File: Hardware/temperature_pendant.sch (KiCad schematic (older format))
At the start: 3 parts

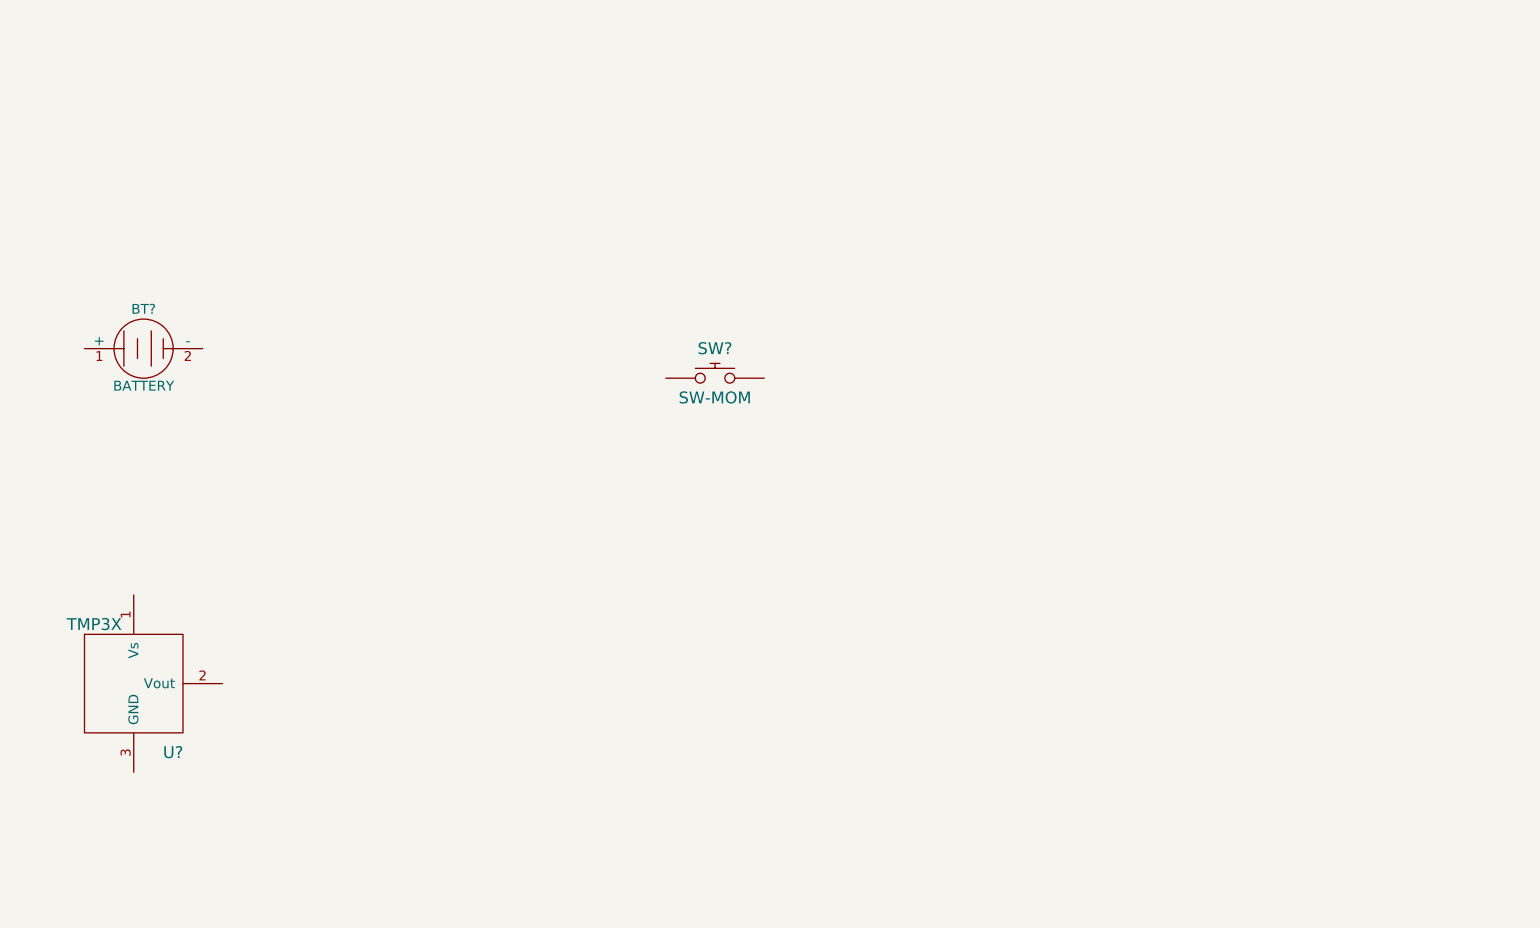
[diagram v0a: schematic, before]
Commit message: Added additional components
Added BlinkM andprogramming header to schematic.
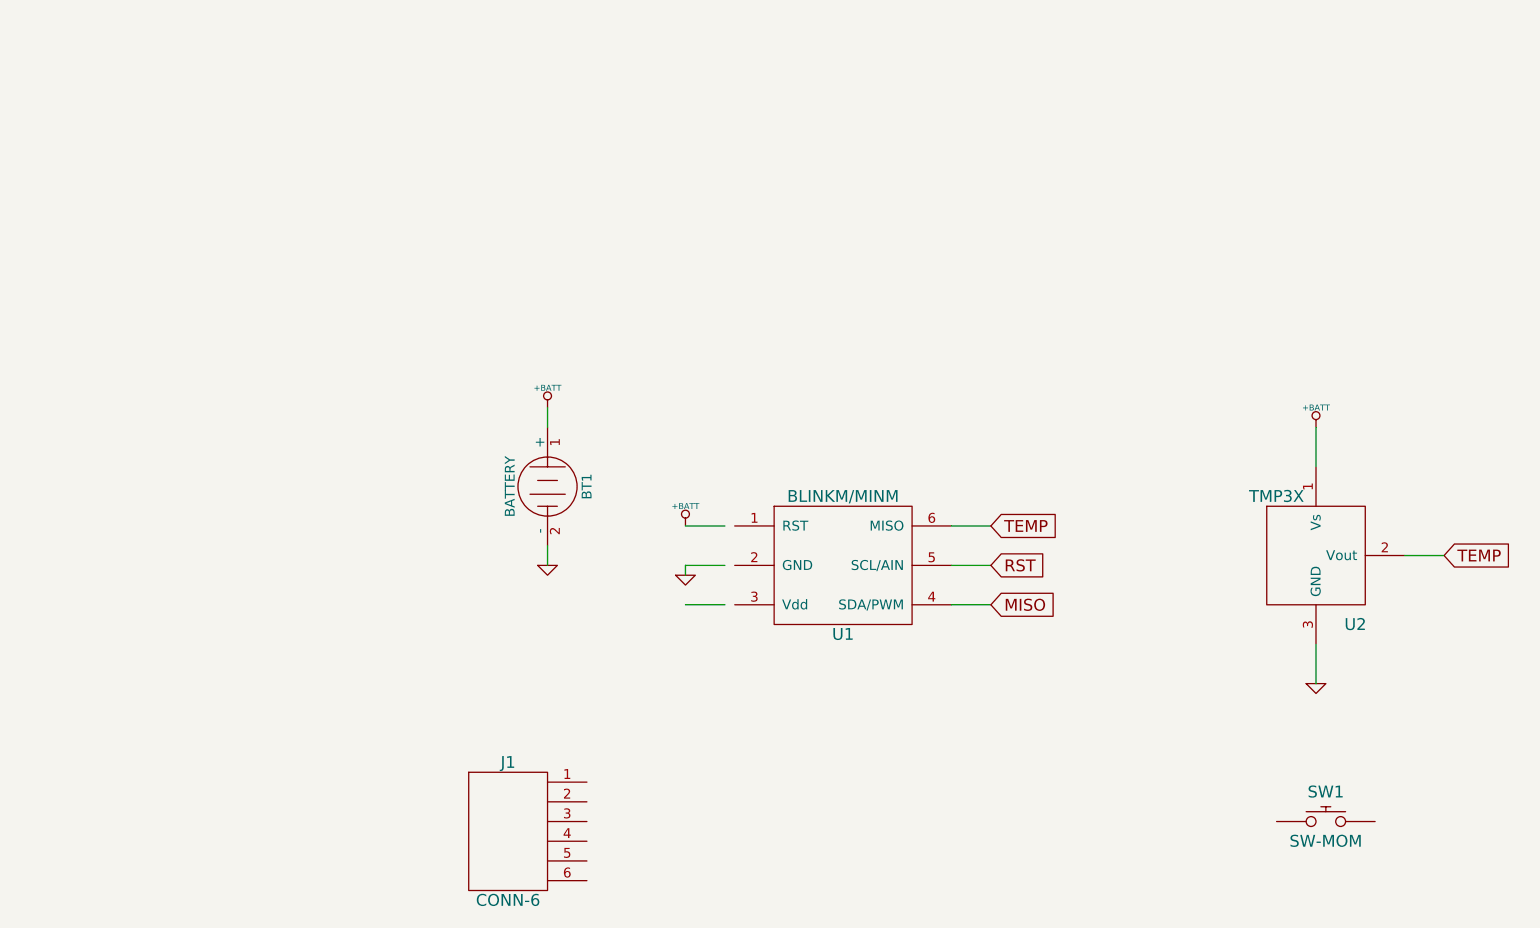
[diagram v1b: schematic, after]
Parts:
- added J1: CONN-6, ~, symbol CONN-6
- added U1: BLINKM/MINM, symbol BLINKM/MINM
- gave numbers to parts that had none: 3
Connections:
- net labels added: +BATT, GND, MISO, RST, TEMP
- wire segments 0 -> 12
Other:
- moved on the sheet: BT1, SW1, U2
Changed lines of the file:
@@
 Sheet 1 1
 Title "Temperature Pendant"
-Date "21 oct 2013"
+Date "22 oct 2013"
 Rev "1"
 Comp "Matthew E. Nelson"
@@
 $EndDescr
 $Comp
-L BATTERY BT?
+L BATTERY BT1
 U 1 1 5264A202
-P 1950 2500
-F 0 "BT?" H 1950 2700 50  0000 C CNN
-F 1 "BATTERY" H 1950 2310 50  0000 C CNN
-F 2 "~" H 1950 2500 60  0000 C CNN
-F 3 "~" H 1950 2500 60  0000 C CNN
-	1    1950 2500
+P 4000 3200
+F 0 "BT1" H 4000 3400 50  0000 C CNN
+F 1 "BATTERY" H 4000 3010 50  0000 C CNN
+F 2 "~" H 4000 3200 60  0000 C CNN
+F 3 "~" H 4000 3200 60  0000 C CNN
+	1    4000 3200
+	0    1    1    0
+$EndComp
+$Comp
+L TMP3X U2
+U 1 1 5264B6FD
+P 7900 3550
+F 0 "U2" H 8100 3200 60  0000 C CNN
+F 1 "TMP3X" H 7700 3850 60  0000 C CNN
+F 2 "" H 7900 3550 60  0000 C CNN
+F 3 "" H 7900 3550 60  0000 C CNN
+	1    7900 3550
 	1    0    0    -1
 $EndComp
 $Comp
-L TMP3X U?
-U 1 1 5264B6FD
-P 1900 4200
-F 0 "U?" H 2100 3850 60  0000 C CNN
-F 1 "TMP3X" H 1700 4500 60  0000 C CNN
-F 2 "" H 1900 4200 60  0000 C CNN
-F 3 "" H 1900 4200 60  0000 C CNN
-	1    1900 4200
+L SW-MOM SW1
+U 1 1 5264B70C
+P 7950 4900
+F 0 "SW1" H 7950 5050 60  0000 C CNN
+F 1 "SW-MOM" H 7950 4800 60  0000 C CNN
+F 2 "~" H 7950 4900 60  0000 C CNN
+F 3 "~" H 7950 4900 60  0000 C CNN
+	1    7950 4900
 	1    0    0    -1
 $EndComp
 $Comp
-L SW-MOM SW?
-U 1 1 5264B70C
-P 4850 2650
-F 0 "SW?" H 4850 2800 60  0000 C CNN
-F 1 "SW-MOM" H 4850 2550 60  0000 C CNN
-F 2 "~" H 4850 2650 60  0000 C CNN
-F 3 "~" H 4850 2650 60  0000 C CNN
-	1    4850 2650
+L BLINKM/MINM U1
+U 1 1 5265EB43
+P 5500 3700
+F 0 "U1" H 5500 3450 60  0000 C CNN
+F 1 "BLINKM/MINM" H 5500 4150 60  0000 C CNN
+F 2 "" H 5500 3700 60  0000 C CNN
+F 3 "" H 5500 3700 60  0000 C CNN
+	1    5500 3700
 	1    0    0    -1
 $EndComp
+Wire Wire Line
+	4000 3500 4000 3600
+$Comp
+L GND #PWR2
+U 1 1 5265EE24
+P 4000 3600
+F 0 "#PWR2" H 4000 3600 30  0001 C CNN
+F 1 "GND" H 4000 3530 30  0001 C CNN
+F 2 "" H 4000 3600 60  0000 C CNN
+F 3 "" H 4000 3600 60  0000 C CNN
+	1    4000 3600
+	1    0    0    -1
+$EndComp
+Wire Wire Line
+	4000 2900 4000 2800
+$Comp
+L +BATT #PWR1
+U 1 1 5265EE65
+P 4000 2800
+F 0 "#PWR1" H 4000 2750 20  0001 C CNN
+F 1 "+BATT" H 4000 2900 30  0000 C CNN
+F 2 "" H 4000 2800 60  0000 C CNN
+F 3 "" H 4000 2800 60  0000 C CNN
+	1    4000 2800
+	1    0    0    -1
+$EndComp
+Wire Wire Line
+	4700 3400 4900 3400
+Wire Wire Line
+	4700 3600 4900 3600
+Wire Wire Line
+	4700 3800 4900 3800
+$Comp
+L +BATT #PWR3
+U 1 1 5265EF91
+P 4700 3400
+F 0 "#PWR3" H 4700 3350 20  0001 C CNN
+F 1 "+BATT" H 4700 3500 30  0000 C CNN
+F 2 "" H 4700 3400 60  0000 C CNN
+F 3 "" H 4700 3400 60  0000 C CNN
+	1    4700 3400
+	1    0    0    -1
+$EndComp
+$Comp
+L GND #PWR4
+U 1 1 5265EFA0
+P 4700 3650
+F 0 "#PWR4" H 4700 3650 30  0001 C CNN
+F 1 "GND" H 4700 3580 30  0001 C CNN
+F 2 "" H 4700 3650 60  0000 C CNN
+F 3 "" H 4700 3650 60  0000 C CNN
+	1    4700 3650
+	1    0    0    -1
+$EndComp
+Wire Wire Line
+	8350 3550 8550 3550
+Text GLabel 8550 3550 2    60   Input ~ 0
+TEMP
+Wire Wire Line
+	7900 4000 7900 4200
+Wire Wire Line
+	7900 2900 7900 3100
+$Comp
+L +BATT #PWR5
+U 1 1 5265F004
+P 7900 2900
+F 0 "#PWR5" H 7900 2850 20  0001 C CNN
+F 1 "+BATT" H 7900 3000 30  0000 C CNN
+F 2 "" H 7900 2900 60  0000 C CNN
+F 3 "" H 7900 2900 60  0000 C CNN
+	1    7900 2900
+	1    0    0    -1
+$EndComp
+$Comp
+L GND #PWR6
+U 1 1 5265F013
+P 7900 4200
+F 0 "#PWR6" H 7900 4200 30  0001 C CNN
+F 1 "GND" H 7900 4130 30  0001 C CNN
+F 2 "" H 7900 4200 60  0000 C CNN
+F 3 "" H 7900 4200 60  0000 C CNN
+	1    7900 4200
+	1    0    0    -1
+$EndComp
+Wire Wire Line
+	4700 3600 4700 3650
+Wire Wire Line
+	6050 3400 6250 3400
+Wire Wire Line
+	6050 3600 6250 3600
+Wire Wire Line
+	6050 3800 6250 3800
+Text GLabel 6250 3400 2    60   Input ~ 0
+TEMP
+Text GLabel 6250 3600 2    60   Input ~ 0
+RST
+Text GLabel 6250 3800 2    60   Input ~ 0
+MISO
+$Comp
+L CONN-6 J1
+U 1 1 5265F63E
+P 3800 4950
+F 0 "J1" H 3800 5300 60  0000 C CNN
+F 1 "CONN-6" H 3800 4600 60  0000 C CNN
+F 2 "~" H 3800 4950 60  0000 C CNN
+F 3 "~" H 3800 4950 60  0000 C CNN
+	1    3800 4950
+	1    0    0    -1
+$EndComp

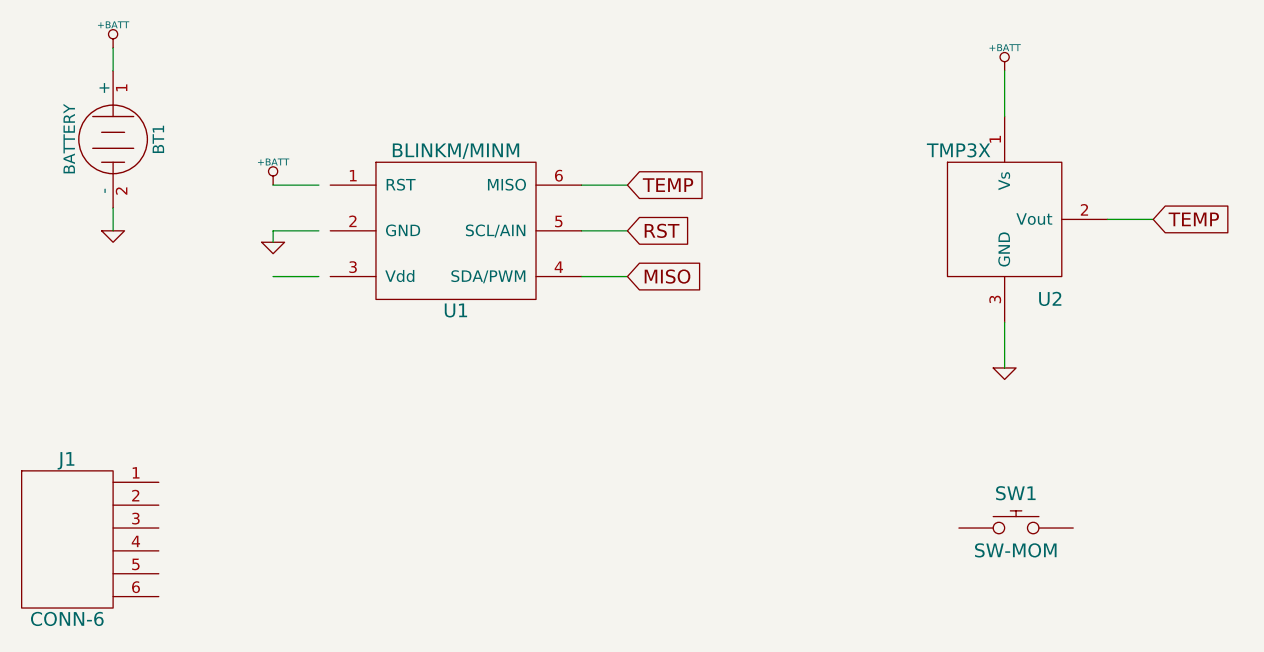
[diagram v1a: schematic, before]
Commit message: Updates
Completed schematic.  Minor revisions, added comments to Arduino code.
Fixed Library reference issue.
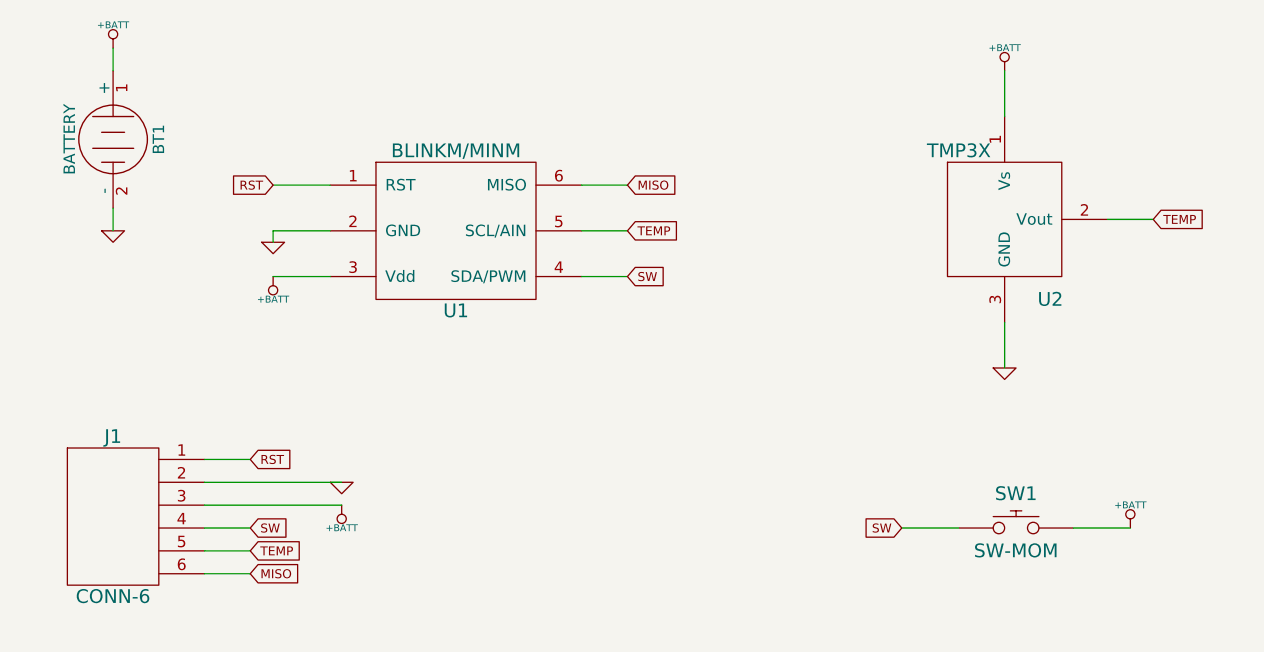
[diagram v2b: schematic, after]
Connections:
- net labels added: SW
- wire segments 12 -> 20
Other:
- moved on the sheet: J1
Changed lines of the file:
@@
 Sheet 1 1
 Title "Temperature Pendant"
-Date "22 oct 2013"
+Date "26 oct 2013"
 Rev "1"
 Comp "Matthew E. Nelson"
@@
 $EndComp
 Wire Wire Line
-	4700 3400 4900 3400
-Wire Wire Line
-	4700 3600 4900 3600
-Wire Wire Line
-	4700 3800 4900 3800
+	4700 3400 4950 3400
+Wire Wire Line
+	4700 3600 4950 3600
+Wire Wire Line
+	4700 3800 4950 3800
 $Comp
 L +BATT #PWR3
 U 1 1 5265EF91
-P 4700 3400
-F 0 "#PWR3" H 4700 3350 20  0001 C CNN
-F 1 "+BATT" H 4700 3500 30  0000 C CNN
-F 2 "" H 4700 3400 60  0000 C CNN
-F 3 "" H 4700 3400 60  0000 C CNN
-	1    4700 3400
-	1    0    0    -1
+P 4700 3800
+F 0 "#PWR3" H 4700 3750 20  0001 C CNN
+F 1 "+BATT" H 4700 3900 30  0000 C CNN
+F 2 "" H 4700 3800 60  0000 C CNN
+F 3 "" H 4700 3800 60  0000 C CNN
+	1    4700 3800
+	1    0    0    1
 $EndComp
 $Comp
@@
 Wire Wire Line
 	8350 3550 8550 3550
-Text GLabel 8550 3550 2    60   Input ~ 0
+Text GLabel 8550 3550 2    39   Input ~ 0
 TEMP
 Wire Wire Line
@@
 Wire Wire Line
 	6050 3800 6250 3800
-Text GLabel 6250 3400 2    60   Input ~ 0
+Text GLabel 6250 3400 2    39   Input ~ 0
+MISO
+Text GLabel 6250 3600 2    39   Input ~ 0
 TEMP
-Text GLabel 6250 3600 2    60   Input ~ 0
-RST
-Text GLabel 6250 3800 2    60   Input ~ 0
-MISO
+Text GLabel 6250 3800 2    39   Input ~ 0
+SW
 $Comp
 L CONN-6 J1
 U 1 1 5265F63E
-P 3800 4950
-F 0 "J1" H 3800 5300 60  0000 C CNN
-F 1 "CONN-6" H 3800 4600 60  0000 C CNN
-F 2 "~" H 3800 4950 60  0000 C CNN
-F 3 "~" H 3800 4950 60  0000 C CNN
-	1    3800 4950
-	1    0    0    -1
-$EndComp
+P 4000 4850
+F 0 "J1" H 4000 5200 60  0000 C CNN
+F 1 "CONN-6" H 4000 4500 60  0000 C CNN
+F 2 "~" H 4000 4850 60  0000 C CNN
+F 3 "~" H 4000 4850 60  0000 C CNN
+	1    4000 4850
+	1    0    0    -1
+$EndComp
+Wire Wire Line
+	7700 4900 7450 4900
+Text GLabel 7450 4900 0    39   Input ~ 0
+SW
+Wire Wire Line
+	8200 4900 8450 4900
+$Comp
+L +BATT #PWR?
+U 1 1 526BECF7
+P 8450 4900
+F 0 "#PWR?" H 8450 4850 20  0001 C CNN
+F 1 "+BATT" H 8450 5000 30  0000 C CNN
+F 2 "" H 8450 4900 60  0000 C CNN
+F 3 "" H 8450 4900 60  0000 C CNN
+	1    8450 4900
+	1    0    0    -1
+$EndComp
+Text GLabel 4700 3400 0    39   Input ~ 0
+RST
+Wire Wire Line
+	4400 4600 4600 4600
+Wire Wire Line
+	4400 4700 5000 4700
+Wire Wire Line
+	4400 4800 5000 4800
+Wire Wire Line
+	4400 4900 4600 4900
+Wire Wire Line
+	4400 5000 4600 5000
+Wire Wire Line
+	4400 5100 4600 5100
+Text GLabel 4600 4600 2    39   Input ~ 0
+RST
+Text GLabel 4600 4900 2    39   Input ~ 0
+SW
+Text GLabel 4600 5000 2    39   Input ~ 0
+TEMP
+Text GLabel 4600 5100 2    39   Input ~ 0
+MISO
+$Comp
+L +BATT #PWR?
+U 1 1 526BEF1C
+P 5000 4800
+F 0 "#PWR?" H 5000 4750 20  0001 C CNN
+F 1 "+BATT" H 5000 4900 30  0000 C CNN
+F 2 "" H 5000 4800 60  0000 C CNN
+F 3 "" H 5000 4800 60  0000 C CNN
+	1    5000 4800
+	1    0    0    1
+$EndComp
+$Comp
+L GND #PWR?
+U 1 1 526BEF30
+P 5000 4700
+F 0 "#PWR?" H 5000 4700 30  0001 C CNN
+F 1 "GND" H 5000 4630 30  0001 C CNN
+F 2 "" H 5000 4700 60  0000 C CNN
+F 3 "" H 5000 4700 60  0000 C CNN
+	1    5000 4700
+	1    0    0    -1
+$EndComp

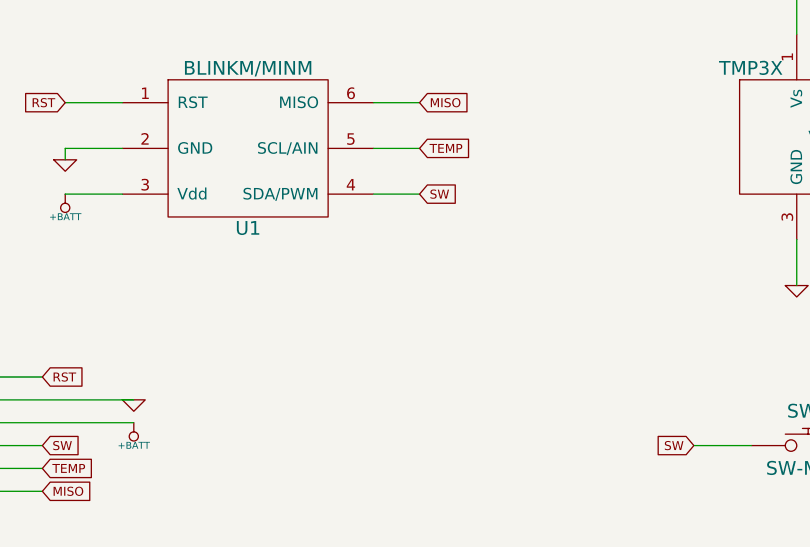
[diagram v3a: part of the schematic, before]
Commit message: Enabled built-in pull ups
Enabled built-in pull down resistor to better stabilize the SW input.
Testing if I still need an external pull-down but for now added one in
the schematic.
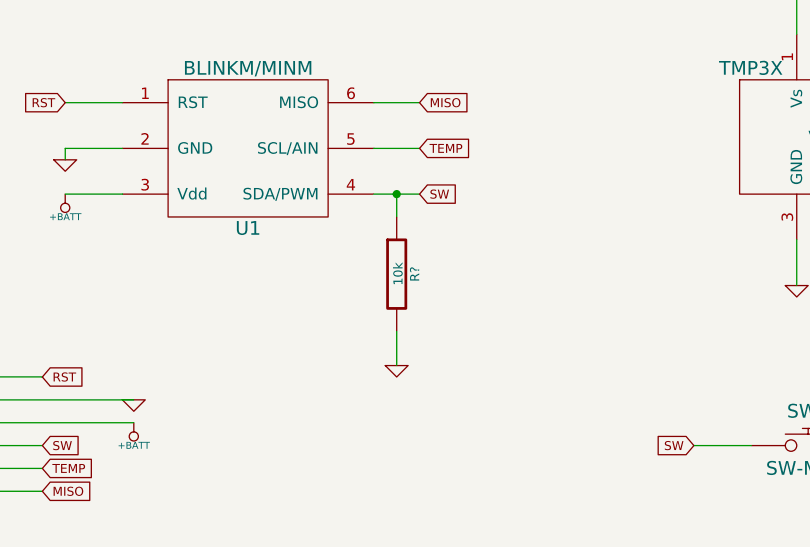
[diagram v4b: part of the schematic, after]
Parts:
- added R?: 10k, ~, symbol R
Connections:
- net GND: now also R?.2
- net SW: now also R?.1
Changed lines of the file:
@@
 Sheet 1 1
 Title "Temperature Pendant"
-Date "26 oct 2013"
+Date "7 dec 2013"
 Rev "1"
 Comp "Matthew E. Nelson"
@@
 	1    0    0    -1
 $EndComp
+$Comp
+L R R?
+U 1 1 52A2BDC6
+P 6150 4150
+F 0 "R?" V 6230 4150 40  0000 C CNN
+F 1 "10k" V 6157 4151 40  0000 C CNN
+F 2 "~" V 6080 4150 30  0000 C CNN
+F 3 "~" H 6150 4150 30  0000 C CNN
+	1    6150 4150
+	1    0    0    -1
+$EndComp
+Wire Wire Line
+	6150 3900 6150 3800
+Connection ~ 6150 3800
+Wire Wire Line
+	6150 4400 6150 4550
+$Comp
+L GND #PWR?
+U 1 1 52A2BE02
+P 6150 4550
+F 0 "#PWR?" H 6150 4550 30  0001 C CNN
+F 1 "GND" H 6150 4480 30  0001 C CNN
+F 2 "" H 6150 4550 60  0000 C CNN
+F 3 "" H 6150 4550 60  0000 C CNN
+	1    6150 4550
+	1    0    0    -1
+$EndComp
